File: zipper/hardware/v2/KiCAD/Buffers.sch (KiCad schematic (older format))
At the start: 20 parts, among them U10 SN74LVC162244A, U13 SN74LVC162244A, U14 SN74LVC162244A, U9 SN74LVC162244A

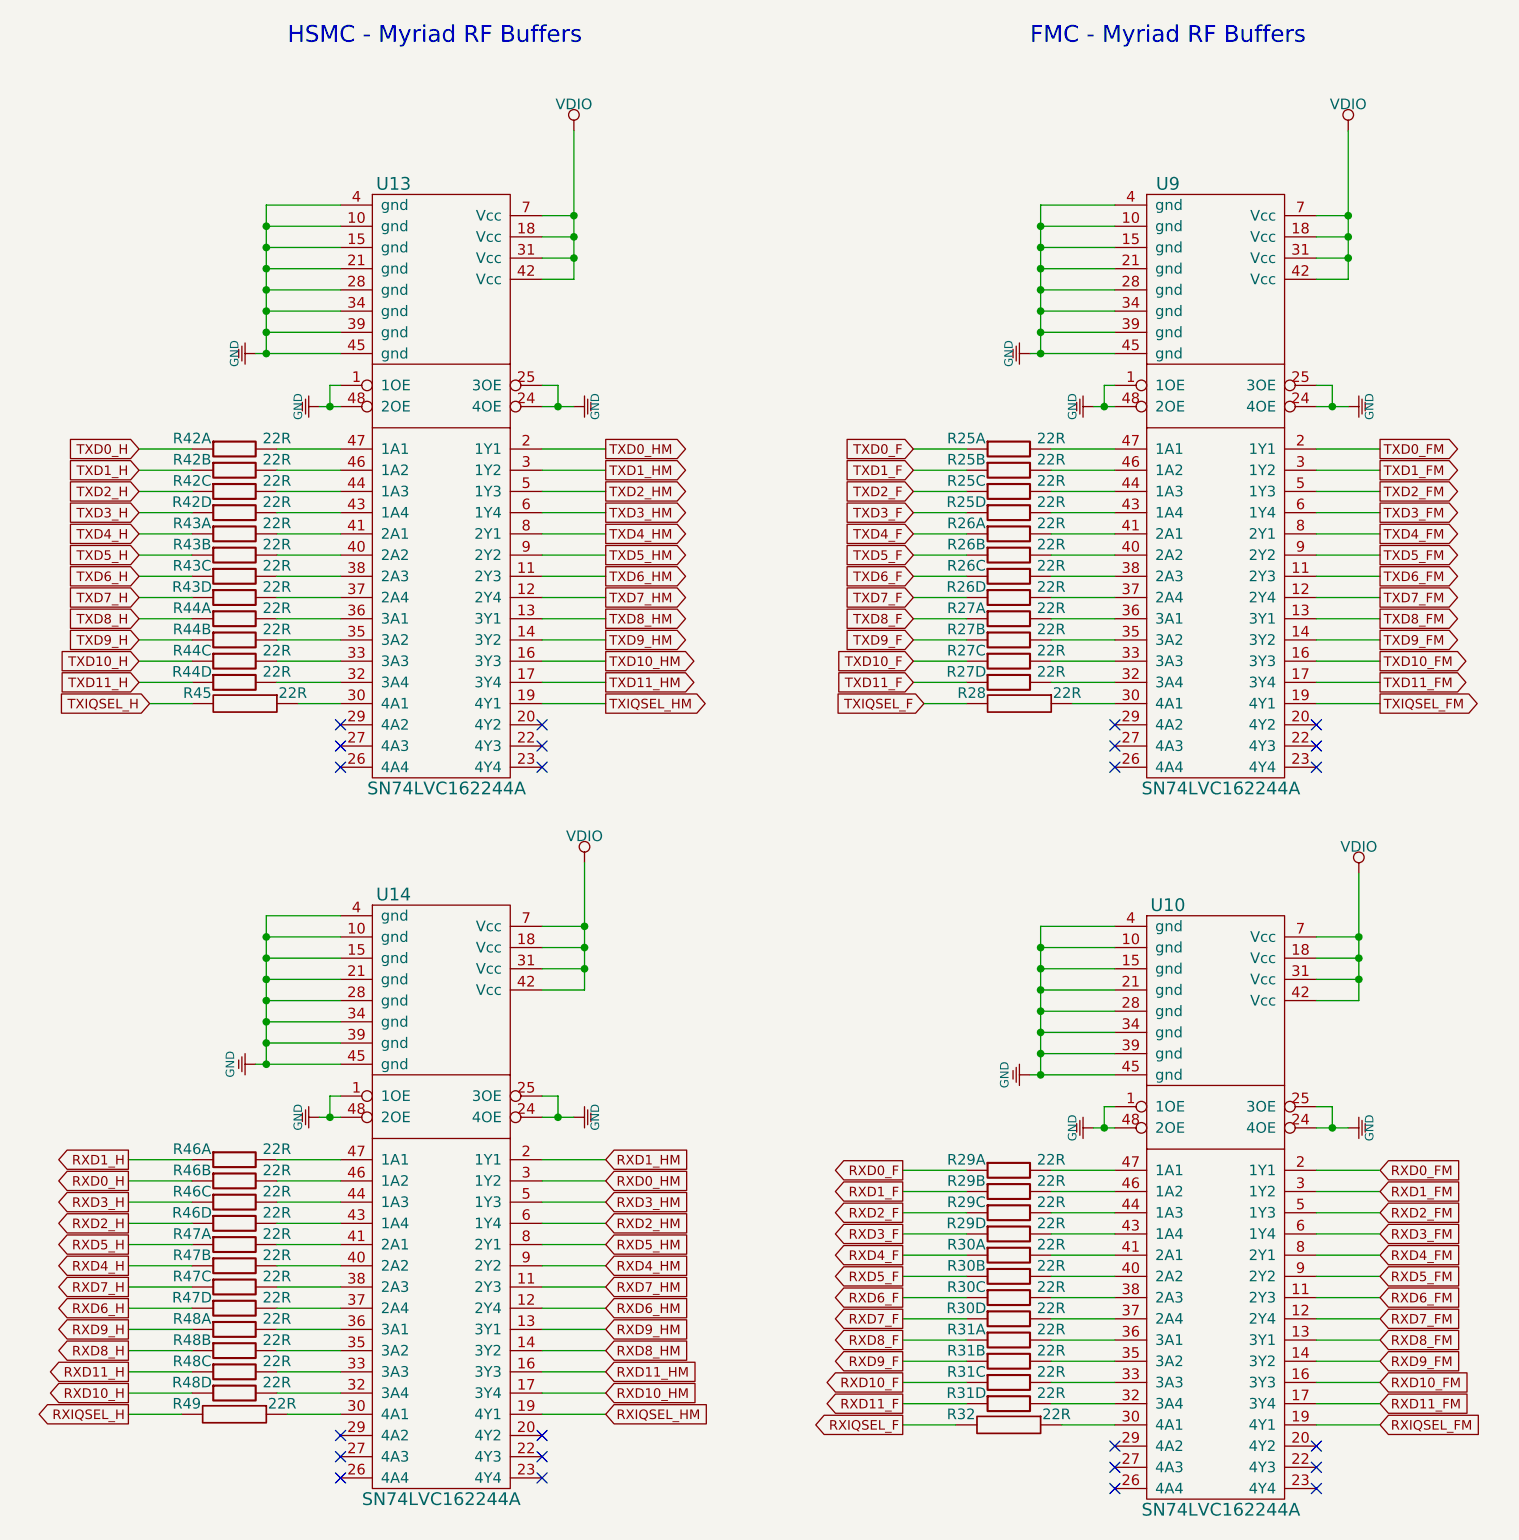
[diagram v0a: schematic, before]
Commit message: Updated dev kit PDF, and hardware design for placement error
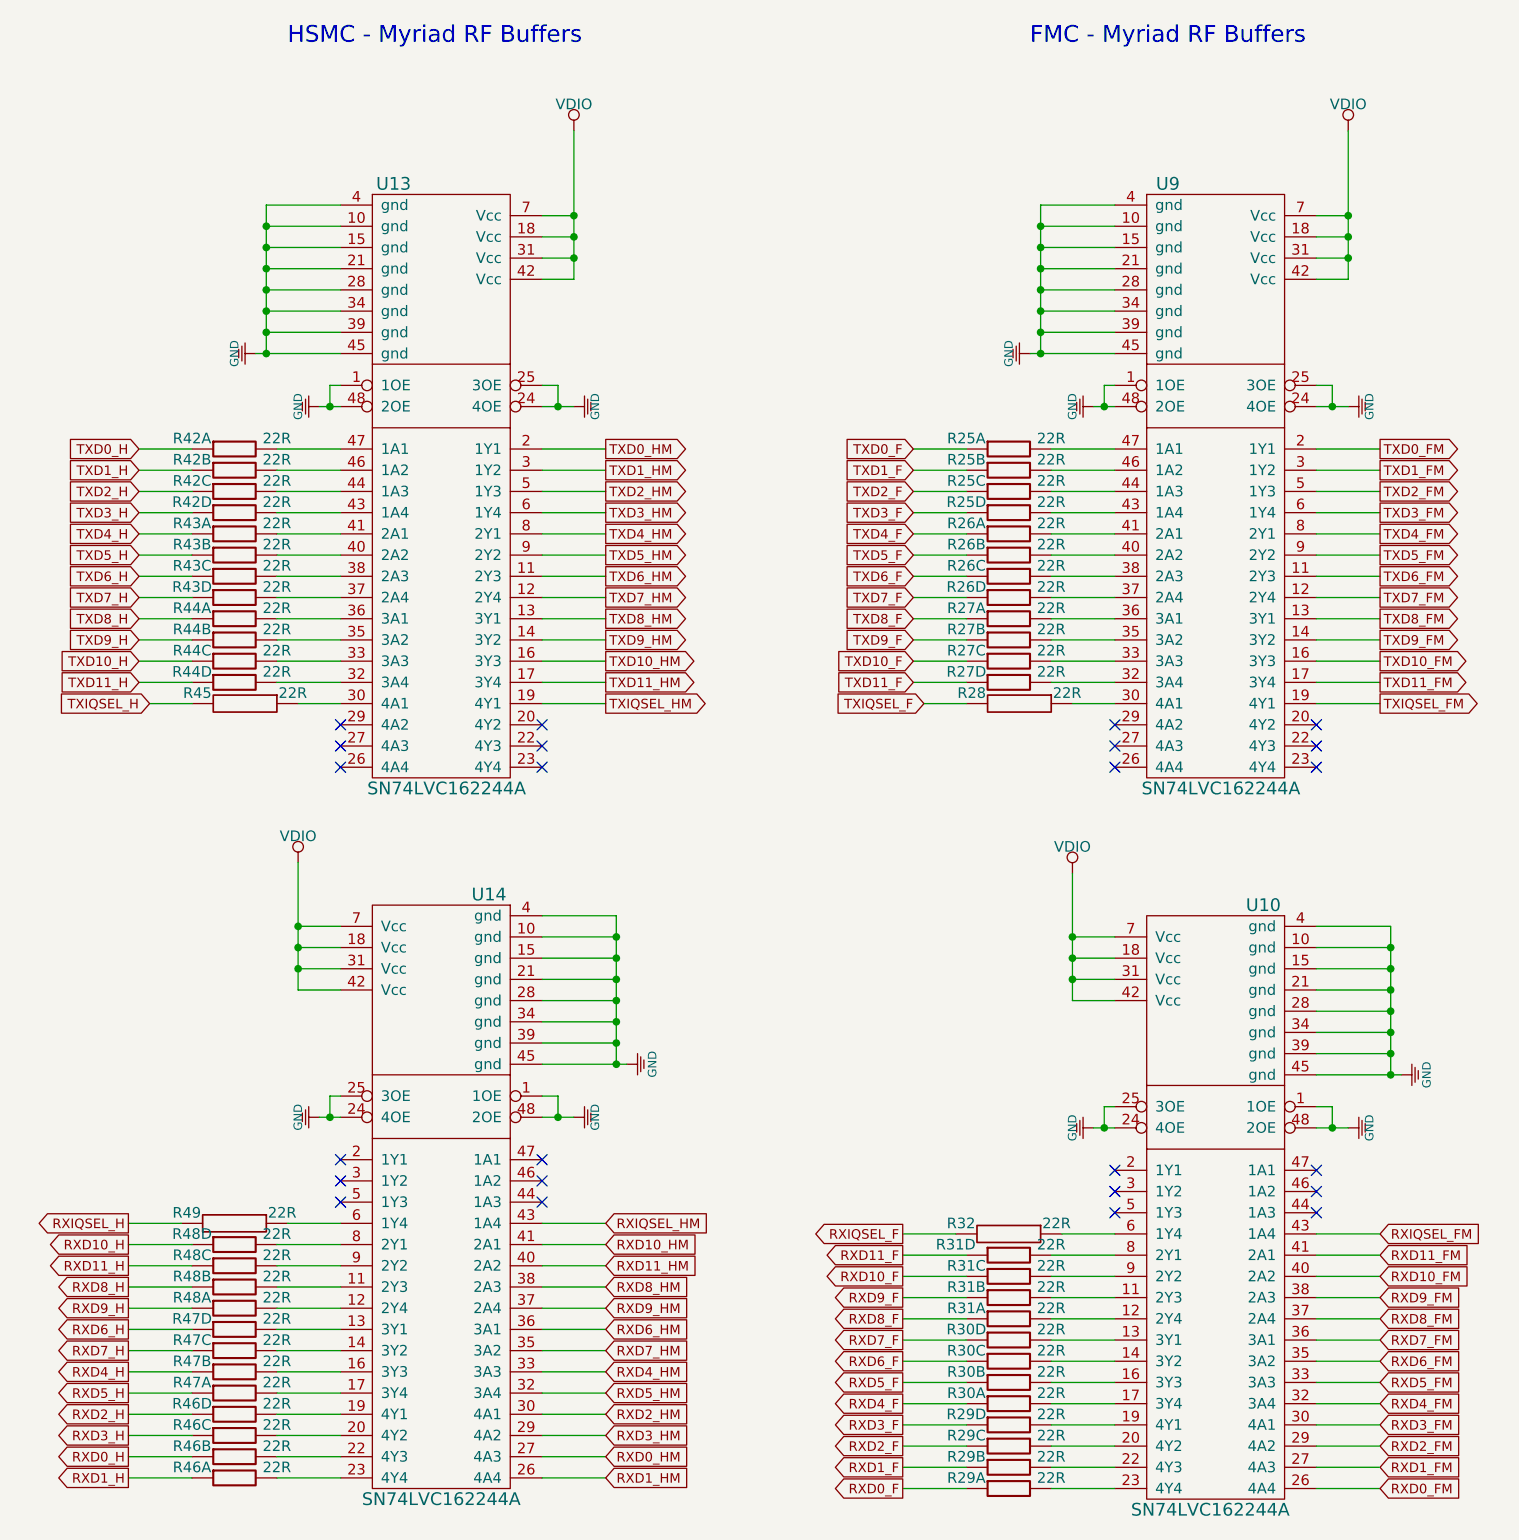
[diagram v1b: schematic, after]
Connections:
- net RXD0_FM: now also U10.26 (4A4); no longer U10.2 (1Y1)
- net RXD0_HM: now also U14.27 (4A3); no longer U14.3 (1Y2)
- net RXD10_FM: now also U10.40 (2A2); no longer U10.16 (3Y3)
- net RXD10_HM: now also U14.41 (2A1); no longer U14.17 (3Y4)
- net RXD11_FM: now also U10.41 (2A1); no longer U10.17 (3Y4)
- net RXD11_HM: now also U14.40 (2A2); no longer U14.16 (3Y3)
- net RXD1_FM: now also U10.27 (4A3); no longer U10.3 (1Y2)
- net RXD1_HM: now also U14.26 (4A4); no longer U14.2 (1Y1)
- net RXD2_FM: now also U10.29 (4A2); no longer U10.5 (1Y3)
- net RXD2_HM: now also U14.30 (4A1); no longer U14.6 (1Y4)
- net RXD3_FM: now also U10.30 (4A1); no longer U10.6 (1Y4)
- net RXD3_HM: now also U14.29 (4A2); no longer U14.5 (1Y3)
- net RXD4_FM: now also U10.32 (3A4); no longer U10.8 (2Y1)
- net RXD4_HM: now also U14.33 (3A3); no longer U14.9 (2Y2)
- net RXD5_FM: now also U10.33 (3A3); no longer U10.9 (2Y2)
- net RXD5_HM: now also U14.32 (3A4); no longer U14.8 (2Y1)
- net RXD6_FM: now also U10.35 (3A2); no longer U10.11 (2Y3)
- net RXD6_HM: now also U14.36 (3A1); no longer U14.12 (2Y4)
- net RXD7_FM: now also U10.36 (3A1); no longer U10.12 (2Y4)
- net RXD7_HM: now also U14.35 (3A2); no longer U14.11 (2Y3)
- net RXD8_FM: now also U10.37 (2A4); no longer U10.13 (3Y1)
- net RXD8_HM: now also U14.38 (2A3); no longer U14.14 (3Y2)
- net RXD9_FM: now also U10.38 (2A3); no longer U10.14 (3Y2)
- net RXD9_HM: now also U14.37 (2A4); no longer U14.13 (3Y1)
- net RXIQSEL_FM: now also U10.43 (1A4); no longer U10.19 (4Y1)
- net RXIQSEL_HM: now also U14.43 (1A4); no longer U14.19 (4Y1)
- net at R46.8: now also U14.23 (4Y4); no longer U14.47 (1A1)
- net at R46.7: now also U14.22 (4Y3); no longer U14.46 (1A2)
- net at R46.6: now also U14.20 (4Y2); no longer U14.44 (1A3)
- net at R46.5: now also U14.19 (4Y1); no longer U14.43 (1A4)
- net at R47.8: now also U14.17 (3Y4); no longer U14.41 (2A1)
- net at R47.7: now also U14.16 (3Y3); no longer U14.40 (2A2)
- net at R47.6: now also U14.14 (3Y2); no longer U14.38 (2A3)
- net at R47.5: now also U14.13 (3Y1); no longer U14.37 (2A4)
- net at R48.8: now also U14.12 (2Y4); no longer U14.36 (3A1)
- net at R48.7: now also U14.11 (2Y3); no longer U14.35 (3A2)
- net at R48.6: now also U14.9 (2Y2); no longer U14.33 (3A3)
- net at R48.5: now also U14.8 (2Y1); no longer U14.32 (3A4)
- net at R29.8: now also U10.23 (4Y4); no longer U10.47 (1A1)
- net at R29.7: now also U10.22 (4Y3); no longer U10.46 (1A2)
- net at R29.6: now also U10.20 (4Y2); no longer U10.44 (1A3)
- net at R29.5: now also U10.19 (4Y1); no longer U10.43 (1A4)
- net at R30.8: now also U10.17 (3Y4); no longer U10.41 (2A1)
- net at R30.7: now also U10.16 (3Y3); no longer U10.40 (2A2)
- net at R30.6: now also U10.14 (3Y2); no longer U10.38 (2A3)
- net at R30.5: now also U10.13 (3Y1); no longer U10.37 (2A4)
- net at R31.8: now also U10.12 (2Y4); no longer U10.36 (3A1)
- net at R31.7: now also U10.11 (2Y3); no longer U10.35 (3A2)
- net at R31.6: now also U10.9 (2Y2); no longer U10.33 (3A3)
- net at R31.5: now also U10.8 (2Y1); no longer U10.32 (3A4)
- net at R49.1: now also U14.6 (1Y4); no longer U14.30 (4A1)
- net at R32.1: now also U10.6 (1Y4); no longer U10.30 (4A1)
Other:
- moved on the sheet: R29A, R29B, R29C, R29D, R30A, R30B, R30C, R30D, R31A, R31B, R31C, R31D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
